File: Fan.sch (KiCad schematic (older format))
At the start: 9 parts, among them Q2 MOSFET_N, Q3 MOSFET_N, Q4 MOSFET_N, U3 MCP4922-E/P, U4 OPA4170

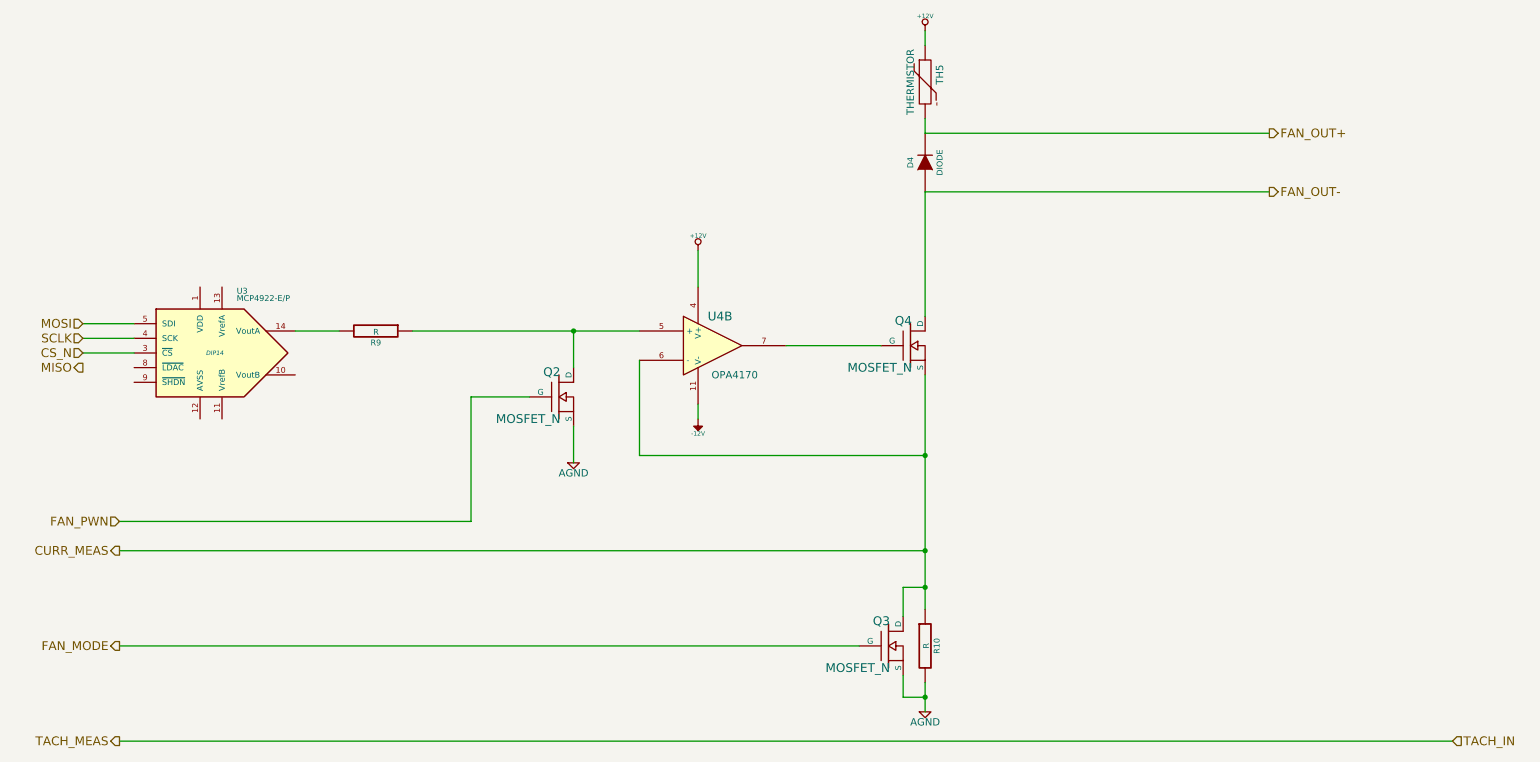
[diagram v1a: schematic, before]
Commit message: 5.7 Video 1/2 Associating and Placing the Arduino Module
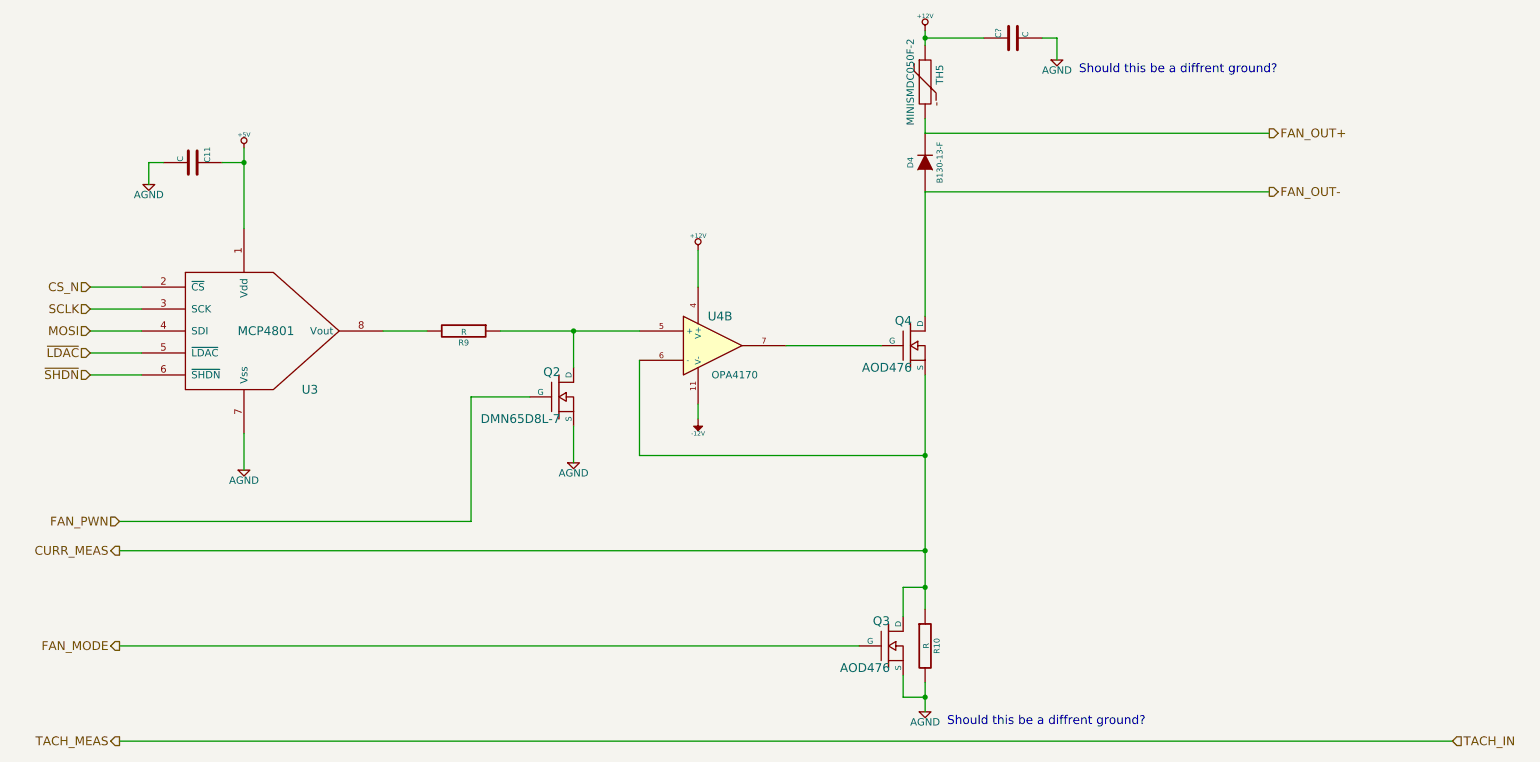
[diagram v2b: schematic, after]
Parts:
- removed U3: MCP4922-E/P, DIP14, symbol MCP4922-E/P
- added C11, C?: C, ~, symbol C
- added U3: MCP4801, symbol MCP4801
- D4: value DIODE -> B130-13-F; MFG Name (none) -> Diodes Inc; MFG Part Number (none) -> B130-13-F
- Q2: value MOSFET_N -> DMN65D8L-7; MFG Name (none) -> Diodes Inc; MFG Part Number (none) -> DMN65D8L-7
- Q3: value MOSFET_N -> AOD476; MFG Name (none) -> Alpha and Omega; MFG Part Number (none) -> AOD476
- Q4: value MOSFET_N -> AOD476; MFG Name (none) -> Alpga and Omega; MFG Part Number (none) -> AOD476
- TH5: value THERMISTOR -> MINISMDC050F-2; MFG Name (none) -> TE Connectivity; MFG Part Number (none) -> MINISMDC050F-2
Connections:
- net +12V: now also C?.1
- net AGND: now also C11.2, C?.2, U3.7 (Vss)
- net CS_N: now also U3.2 (~CS)
- net MOSI: now also U3.4 (SDI)
- net SCLK: now also U3.3 (SCK)
- net at R9.2: now also U3.8 (Vout)
- new net +5V: C11.1, U3.1 (Vdd)
- new net ~LDAC: U3.5 (~LDAC)
- new net ~SHDN: U3.6 (~SHDN)
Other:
- note added: "Should this be a diffrent ground?"
- moved on the sheet: R9
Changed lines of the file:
@@
 Sheet 6 9
 Title ""
-Date "22 feb 2014"
+Date "23 feb 2014"
 Rev ""
 Comp ""
@@
 P 6650 2800
 F 0 "Q4" H 6660 2970 60  0000 R CNN
-F 1 "MOSFET_N" H 6660 2650 60  0000 R CNN
+F 1 "AOD476" H 6660 2650 60  0000 R CNN
 F 2 "" H 6650 2800 60  0000 C CNN
 F 3 "" H 6650 2800 60  0000 C CNN
+F 4 "Alpga and Omega" H 6650 2800 60  0001 C CNN "MFG Name"
+F 5 "AOD476" H 6650 2800 60  0001 C CNN "MFG Part Number"
 	1    6650 2800
 	1    0    0    -1
 $EndComp
 $Comp
-L +12V #PWR023
+L +12V #PWR29
 U 1 1 52F26B42
 P 6750 650
-F 0 "#PWR023" H 6750 600 20  0001 C CNN
+F 0 "#PWR29" H 6750 600 20  0001 C CNN
 F 1 "+12V" H 6750 750 30  0000 C CNN
 F 2 "" H 6750 650 60  0000 C CNN
@@
 $EndComp
 $Comp
-L AGND #PWR024
+L AGND #PWR30
 U 1 1 52F26B7F
 P 6750 5300
-F 0 "#PWR024" H 6750 5300 40  0001 C CNN
+F 0 "#PWR30" H 6750 5300 40  0001 C CNN
 F 1 "AGND" H 6750 5230 50  0000 C CNN
 F 2 "" H 6750 5300 60  0000 C CNN
@@
 $EndComp
 $Comp
-L +12V #PWR025
+L +12V #PWR27
 U 1 1 52F26BE2
 P 5200 2150
-F 0 "#PWR025" H 5200 2100 20  0001 C CNN
+F 0 "#PWR27" H 5200 2100 20  0001 C CNN
 F 1 "+12V" H 5200 2250 30  0000 C CNN
 F 2 "" H 5200 2150 60  0000 C CNN
@@
 $EndComp
 $Comp
-L -12V #PWR026
+L -12V #PWR28
 U 1 1 52F26BF3
 P 5200 3300
-F 0 "#PWR026" H 5200 3430 20  0001 C CNN
+F 0 "#PWR28" H 5200 3430 20  0001 C CNN
 F 1 "-12V" H 5200 3400 30  0000 C CNN
 F 2 "" H 5200 3300 60  0000 C CNN
@@
 $EndComp
 $Comp
-L AGND #PWR027
+L AGND #PWR26
 U 1 1 52F26C6F
 P 4350 3600
-F 0 "#PWR027" H 4350 3600 40  0001 C CNN
+F 0 "#PWR26" H 4350 3600 40  0001 C CNN
 F 1 "AGND" H 4350 3530 50  0000 C CNN
 F 2 "" H 4350 3600 60  0000 C CNN
@@
 	1    0    0    -1
 $EndComp
-$Comp
-L MCP4922-E/P U3
-U 1 1 52F26C9B
-P 1900 2850
-F 0 "U3" H 2050 3250 40  0000 L BNN
-F 1 "MCP4922-E/P" H 2050 3200 40  0000 L BNN
-F 2 "DIP14" H 1900 2850 30  0000 C CIN
-F 3 "" H 1900 2850 60  0000 C CNN
-	1    1900 2850
-	1    0    0    -1
-$EndComp
 Text HLabel 1250 4200 0    60   Output ~ 0
 CURR_MEAS
@@
 L R R9
 U 1 1 52F26DC7
-P 3000 2700
-F 0 "R9" V 3080 2700 40  0000 C CNN
-F 1 "R" V 3007 2701 40  0000 C CNN
-F 2 "" V 2930 2700 30  0000 C CNN
-F 3 "" H 3000 2700 30  0000 C CNN
-	1    3000 2700
+P 3600 2700
+F 0 "R9" V 3680 2700 40  0000 C CNN
+F 1 "R" V 3607 2701 40  0000 C CNN
+F 2 "" V 3530 2700 30  0000 C CNN
+F 3 "" H 3600 2700 30  0000 C CNN
+	1    3600 2700
 	0    1    1    0
 $EndComp
-Text HLabel 1000 2650 0    60   Input ~ 0
+Text HLabel 1050 2700 0    60   Input ~ 0
 MOSI
-Text HLabel 1000 2950 0    60   Output ~ 0
-MISO
-Text HLabel 1000 2850 0    60   Input ~ 0
+Text HLabel 1050 2400 0    60   Input ~ 0
 CS_N
-Text HLabel 1000 2750 0    60   Input ~ 0
+Text HLabel 1050 2550 0    60   Input ~ 0
 SCLK
 $Comp
@@
 P 4250 3150
 F 0 "Q2" H 4260 3320 60  0000 R CNN
-F 1 "MOSFET_N" H 4260 3000 60  0000 R CNN
+F 1 "DMN65D8L-7" H 4260 3000 60  0000 R CNN
 F 2 "~" H 4250 3150 60  0000 C CNN
 F 3 "~" H 4250 3150 60  0000 C CNN
+F 4 "Diodes Inc" H 4250 3150 60  0001 C CNN "MFG Name"
+F 5 "DMN65D8L-7" H 4250 3150 60  0001 C CNN "MFG Part Number"
 	1    4250 3150
 	1    0    0    -1
@@
 P 6750 1550
 F 0 "D4" H 6750 1650 40  0000 C CNN
-F 1 "DIODE" H 6750 1450 40  0000 C CNN
+F 1 "B130-13-F" H 6750 1450 40  0000 C CNN
 F 2 "~" H 6750 1550 60  0000 C CNN
 F 3 "~" H 6750 1550 60  0000 C CNN
+F 4 "Diodes Inc" H 6750 1550 60  0001 C CNN "MFG Name"
+F 5 "B130-13-F" H 6750 1550 60  0001 C CNN "MFG Part Number"
 	1    6750 1550
 	0    -1   -1   0
@@
 P 6500 4850
 F 0 "Q3" H 6510 5020 60  0000 R CNN
-F 1 "MOSFET_N" H 6510 4700 60  0000 R CNN
+F 1 "AOD476" H 6510 4700 60  0000 R CNN
 F 2 "~" H 6500 4850 60  0000 C CNN
 F 3 "~" H 6500 4850 60  0000 C CNN
+F 4 "Alpha and Omega" H 6500 4850 60  0001 C CNN "MFG Name"
+F 5 "AOD476" H 6500 4850 60  0001 C CNN "MFG Part Number"
 	1    6500 4850
 	1    0    0    -1
@@
 	5200 3200 5200 3300
 Wire Wire Line
-	3250 2700 4800 2700
+	3850 2700 4800 2700
 Wire Wire Line
 	4350 2700 4350 2950
@@
 Wire Wire Line
 	6750 4200 1250 4200
-Wire Wire Line
-	2450 2700 2750 2700
 Connection ~ 4350 2700
 Wire Wire Line
-	1000 2650 1350 2650
-Wire Wire Line
-	1000 2750 1350 2750
-Wire Wire Line
-	1000 2850 1350 2850
+	1050 2700 1400 2700
 Wire Wire Line
 	4350 3350 4350 3600
@@
 P 6750 1000
 F 0 "TH5" V 6850 1050 50  0000 C CNN
-F 1 "THERMISTOR" V 6650 1000 50  0000 C CNN
+F 1 "MINISMDC050F-2" V 6650 1000 50  0000 C CNN
 F 2 "~" H 6750 1000 60  0000 C CNN
 F 3 "~" H 6750 1000 60  0000 C CNN
+F 4 "TE Connectivity" H 6750 1000 60  0001 C CNN "MFG Name"
+F 5 "MINISMDC050F-2" H 6750 1000 60  0001 C CNN "MFG Part Number"
 	1    6750 1000
 	1    0    0    -1
@@
 Wire Wire Line
 	6750 750  6750 650
+$Comp
+L MCP4801 U3
+U 1 1 530A346F
+P 2000 2300
+F 0 "U3" H 2550 1500 60  0000 C CNN
+F 1 "MCP4801" H 2250 1900 60  0000 C CNN
+F 2 "" H 2000 2300 60  0000 C CNN
+F 3 "" H 2000 2300 60  0000 C CNN
+	1    2000 2300
+	1    0    0    -1
+$EndComp
+Wire Wire Line
+	3050 2700 3350 2700
+Wire Wire Line
+	1400 2400 1050 2400
+Wire Wire Line
+	1050 2550 1400 2550
+Text HLabel 1050 2850 0    60   Input ~ 0
+~LDAC
+Text HLabel 1050 3000 0    60   Input ~ 0
+~SHDN
+Wire Wire Line
+	1400 2850 1050 2850
+Wire Wire Line
+	1050 3000 1400 3000
+$Comp
+L +5V #PWR24
+U 1 1 530AA93A
+P 2100 1450
+F 0 "#PWR24" H 2100 1540 20  0001 C CNN
+F 1 "+5V" H 2100 1540 30  0000 C CNN
+F 2 "" H 2100 1450 60  0000 C CNN
+F 3 "" H 2100 1450 60  0000 C CNN
+	1    2100 1450
+	-1   0    0    -1
+$EndComp
+Wire Wire Line
+	2100 1450 2100 2000
+$Comp
+L C C11
+U 1 1 530AA941
+P 1750 1550
+F 0 "C11" H 1750 1650 40  0000 L CNN
+F 1 "C" H 1756 1465 40  0000 L CNN
+F 2 "~" H 1788 1400 30  0000 C CNN
+F 3 "~" H 1750 1550 60  0000 C CNN
+	1    1750 1550
+	0    1    -1   0
+$EndComp
+Wire Wire Line
+	1950 1550 2100 1550
+Connection ~ 2100 1550
+$Comp
+L AGND #PWR23
+U 1 1 530AA949
+P 1450 1700
+F 0 "#PWR23" H 1450 1700 40  0001 C CNN
+F 1 "AGND" H 1450 1630 50  0000 C CNN
+F 2 "" H 1450 1700 60  0000 C CNN
+F 3 "" H 1450 1700 60  0000 C CNN
+	1    1450 1700
+	-1   0    0    -1
+$EndComp
+Wire Wire Line
+	1550 1550 1450 1550
+Wire Wire Line
+	1450 1550 1450 1700
+$Comp
+L AGND #PWR25
+U 1 1 530AA932
+P 2100 3650
+F 0 "#PWR25" H 2100 3650 40  0001 C CNN
+F 1 "AGND" H 2100 3580 50  0000 C CNN
+F 2 "" H 2100 3650 60  0000 C CNN
+F 3 "" H 2100 3650 60  0000 C CNN
+	1    2100 3650
+	1    0    0    -1
+$EndComp
+Wire Wire Line
+	2100 3400 2100 3650
+$Comp
+L C C?
+U 1 1 530AAAE4
+P 7350 700
+F 0 "C?" H 7350 800 40  0000 L CNN
+F 1 "C" H 7356 615 40  0000 L CNN
+F 2 "~" H 7388 550 30  0000 C CNN
+F 3 "~" H 7350 700 60  0000 C CNN
+	1    7350 700
+	0    -1   -1   0
+$EndComp
+Wire Wire Line
+	6750 700  7150 700
+$Comp
+L AGND #PWR?
+U 1 1 530AAAEC
+P 7650 850
+F 0 "#PWR?" H 7650 850 40  0001 C CNN
+F 1 "AGND" H 7650 780 50  0000 C CNN
+F 2 "" H 7650 850 60  0000 C CNN
+F 3 "" H 7650 850 60  0000 C CNN
+	1    7650 850
+	1    0    0    -1
+$EndComp
+Wire Wire Line
+	7550 700  7650 700
+Wire Wire Line
+	7650 700  7650 850
+Connection ~ 6750 700
+Text Notes 7800 950  0    60   ~ 0
+Should this be a diffrent ground?
+Text Notes 6900 5400 0    60   ~ 0
+Should this be a diffrent ground?
 $EndSCHEMATC

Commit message: 5.7 Video 2/2 Associating and Placing the Arduino Module
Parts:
- removed Q3: AOD476, ~, symbol MOSFET_N
- removed Q4: AOD476, symbol MOSFET_N
- added Q3, Q4: AOD476, ~, symbol MOS_N_NUM
- gave numbers to parts that had none: 1
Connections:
- net AGND: now also Q3.3 (S)
- net CURR_MEAS: now also Q3.2 (D), Q4.3 (S)
- net FAN_MODE: now also Q3.1 (G)
- net FAN_OUT-: now also Q4.2 (D)
- net at U4.7: now also Q4.1 (G)
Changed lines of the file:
@@
-$EndComp
-$Comp
-L MOSFET_N Q4
-U 1 1 52F26B33
-P 6650 2800
-F 0 "Q4" H 6660 2970 60  0000 R CNN
-F 1 "AOD476" H 6660 2650 60  0000 R CNN
-F 2 "" H 6650 2800 60  0000 C CNN
-F 3 "" H 6650 2800 60  0000 C CNN
-F 4 "Alpga and Omega" H 6650 2800 60  0001 C CNN "MFG Name"
-F 5 "AOD476" H 6650 2800 60  0001 C CNN "MFG Part Number"
-	1    6650 2800
-	1    0    0    -1
 $EndComp
 $Comp
@@
 	0    -1   -1   0
 $EndComp
-$Comp
-L MOSFET_N Q3
-U 1 1 52F82F64
-P 6500 4850
-F 0 "Q3" H 6510 5020 60  0000 R CNN
-F 1 "AOD476" H 6510 4700 60  0000 R CNN
-F 2 "~" H 6500 4850 60  0000 C CNN
-F 3 "~" H 6500 4850 60  0000 C CNN
-F 4 "Alpha and Omega" H 6500 4850 60  0001 C CNN "MFG Name"
-F 5 "AOD476" H 6500 4850 60  0001 C CNN "MFG Part Number"
-	1    6500 4850
-	1    0    0    -1
-$EndComp
 Wire Wire Line
 	6750 3000 6750 4600
@@
 	6750 1350 6750 1250
 Wire Wire Line
-	6750 750  6750 650
+	6750 650  6750 750
 $Comp
 L MCP4801 U3
@@
 	2100 3400 2100 3650
 $Comp
-L C C?
+L C C12
 U 1 1 530AAAE4
 P 7350 700
-F 0 "C?" H 7350 800 40  0000 L CNN
+F 0 "C12" H 7350 800 40  0000 L CNN
 F 1 "C" H 7356 615 40  0000 L CNN
 F 2 "~" H 7388 550 30  0000 C CNN
@@
 	6750 700  7150 700
 $Comp
-L AGND #PWR?
+L AGND #PWR31
 U 1 1 530AAAEC
 P 7650 850
-F 0 "#PWR?" H 7650 850 40  0001 C CNN
+F 0 "#PWR31" H 7650 850 40  0001 C CNN
 F 1 "AGND" H 7650 780 50  0000 C CNN
 F 2 "" H 7650 850 60  0000 C CNN
@@
 Text Notes 6900 5400 0    60   ~ 0
 Should this be a diffrent ground?
+$Comp
+L MOS_N_NUM Q3
+U 1 1 530A49C9
+P 6500 4850
+F 0 "Q3" H 6510 5020 60  0000 R CNN
+F 1 "AOD476" H 6510 4700 60  0000 R CNN
+F 2 "~" H 6500 4850 60  0000 C CNN
+F 3 "~" H 6500 4850 60  0000 C CNN
+F 4 "Alpha and Omega" H 6500 4850 60  0001 C CNN "MFG Name"
+F 5 "AOD476" H 6500 4850 60  0001 C CNN "MFG Part Number"
+	1    6500 4850
+	1    0    0    -1
+$EndComp
+$Comp
+L MOS_N_NUM Q4
+U 1 1 530A49DF
+P 6650 2800
+F 0 "Q4" H 6660 2970 60  0000 R CNN
+F 1 "AOD476" H 6660 2650 60  0000 R CNN
+F 2 "~" H 6650 2800 60  0000 C CNN
+F 3 "~" H 6650 2800 60  0000 C CNN
+F 4 "Alpha and Omega" H 6650 2800 60  0001 C CNN "MFG Name"
+F 5 "AOD476" H 6650 2800 60  0001 C CNN "MFG Part Number"
+	1    6650 2800
+	1    0    0    -1
+$EndComp
 $EndSCHEMATC
